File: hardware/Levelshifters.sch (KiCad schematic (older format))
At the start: 36 parts, among them U1401 SN74AXC8T245, U1402 SN74AXC8T245, U1403 SN74AXC8T245, U1404 LSF0102, U1405 LSF0102

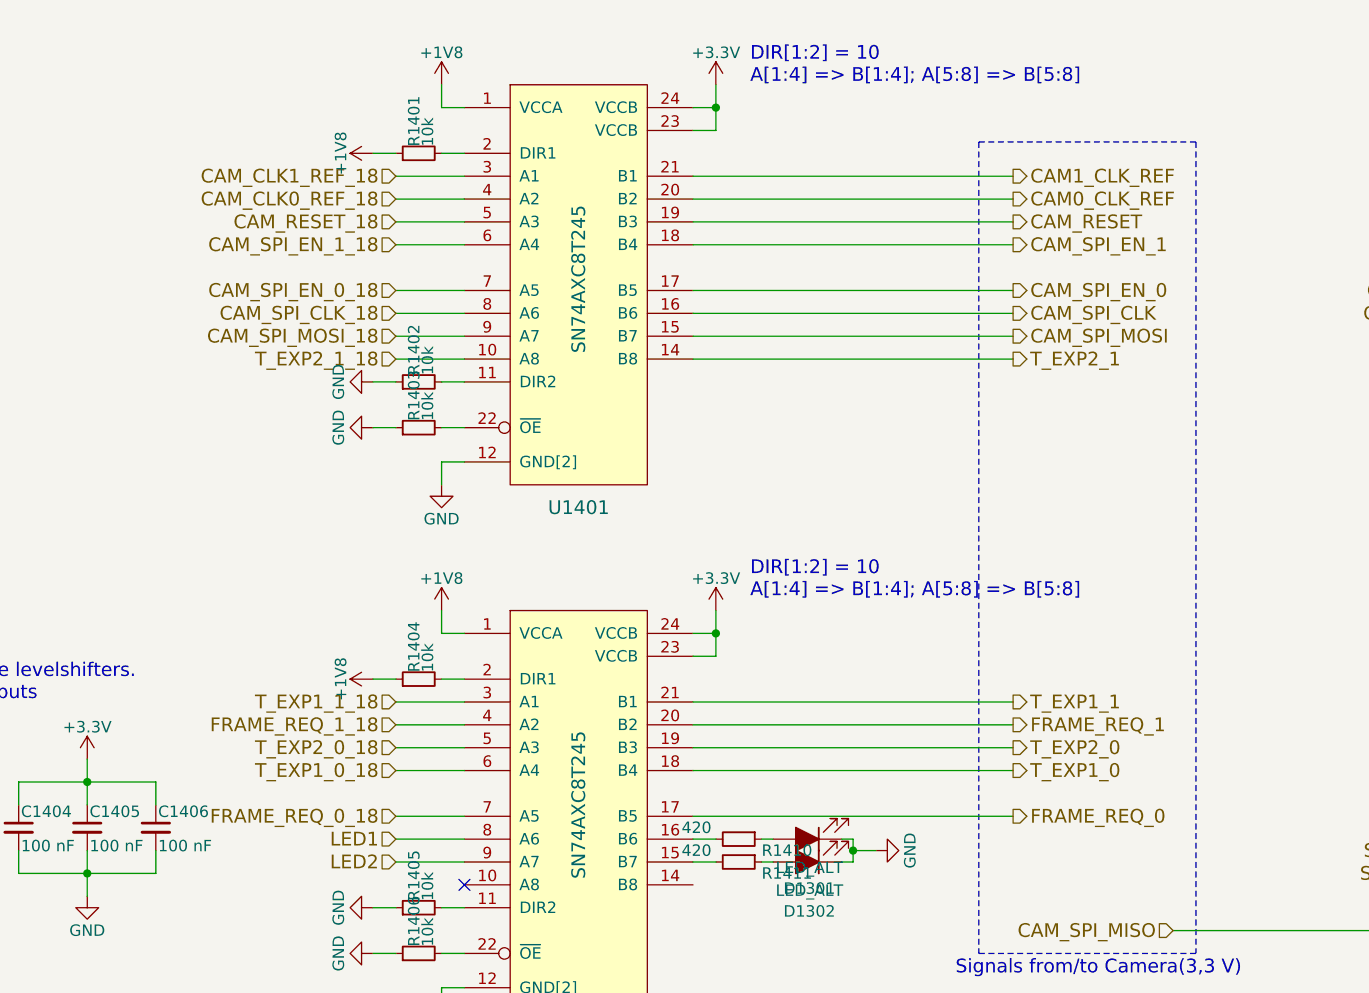
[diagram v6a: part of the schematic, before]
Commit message: WIP: route GPIOs/Levelshifters
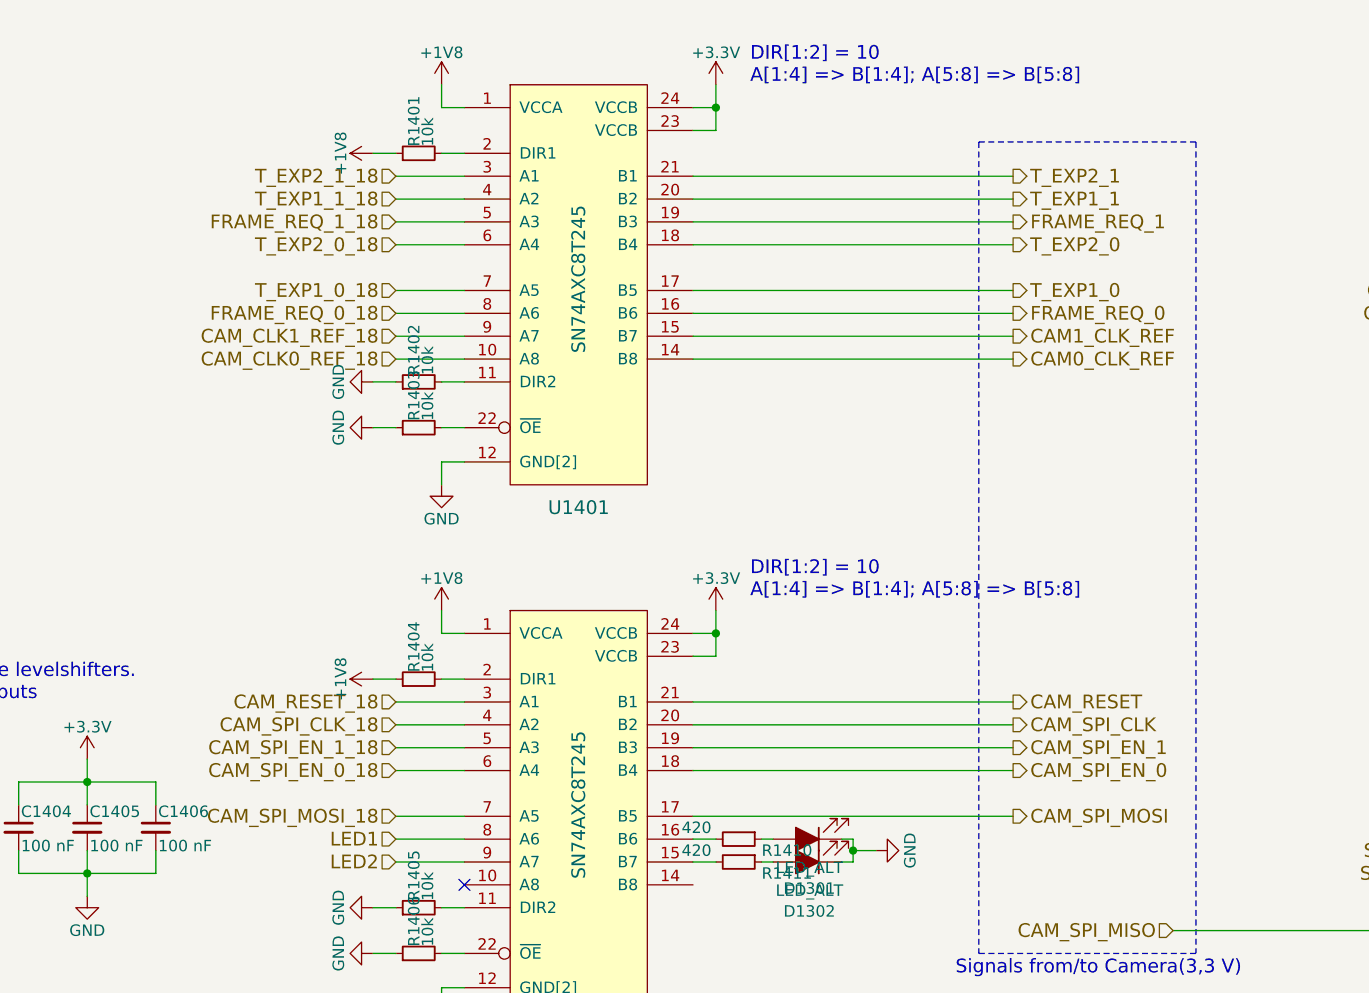
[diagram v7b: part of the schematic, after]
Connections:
- net CAM0_CLK_REF: now also U1401.14 (B8); no longer U1401.20 (B2)
- net CAM1_CLK_REF: now also U1401.15 (B7); no longer U1401.21 (B1)
- net CAM_CLK0_REF_18: now also U1401.10 (A8); no longer U1401.4 (A2)
- net CAM_CLK1_REF_18: now also U1401.9 (A7); no longer U1401.3 (A1)
- net CAM_RESET: now also U1402.21 (B1); no longer U1401.19 (B3)
- net CAM_RESET_18: now also U1402.3 (A1); no longer U1401.5 (A3)
- net CAM_SPI_CLK: now also U1402.20 (B2); no longer U1401.16 (B6)
- net CAM_SPI_CLK_18: now also U1402.4 (A2); no longer U1401.8 (A6)
- net CAM_SPI_EN_0: now also U1402.18 (B4); no longer U1401.17 (B5)
- net CAM_SPI_EN_0_18: now also U1402.6 (A4); no longer U1401.7 (A5)
- net CAM_SPI_EN_1: now also U1402.19 (B3); no longer U1401.18 (B4)
- net CAM_SPI_EN_1_18: now also U1402.5 (A3); no longer U1401.6 (A4)
- net CAM_SPI_MOSI: now also U1402.17 (B5); no longer U1401.15 (B7)
- net CAM_SPI_MOSI_18: now also U1402.7 (A5); no longer U1401.9 (A7)
- net FRAME_REQ_0: now also U1401.16 (B6); no longer U1402.17 (B5)
- net FRAME_REQ_0_18: now also U1401.8 (A6); no longer U1402.7 (A5)
- net FRAME_REQ_1: now also U1401.19 (B3); no longer U1402.20 (B2)
- net FRAME_REQ_1_18: now also U1401.5 (A3); no longer U1402.4 (A2)
- net T_EXP1_0: now also U1401.17 (B5); no longer U1402.18 (B4)
- net T_EXP1_0_18: now also U1401.7 (A5); no longer U1402.6 (A4)
- net T_EXP1_1: now also U1401.20 (B2); no longer U1402.21 (B1)
- net T_EXP1_1_18: now also U1401.4 (A2); no longer U1402.3 (A1)
- net T_EXP2_0: now also U1401.18 (B4); no longer U1402.19 (B3)
- net T_EXP2_0_18: now also U1401.6 (A4); no longer U1402.5 (A3)
- net T_EXP2_1: now also U1401.21 (B1); no longer U1401.14 (B8)
- net T_EXP2_1_18: now also U1401.3 (A1); no longer U1401.10 (A8)
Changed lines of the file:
@@
 Text HLabel 10600 1800 2    60   BiDi ~ 0
 CAM_SCL
+Text HLabel 5950 1900 2    60   Output ~ 0
+FRAME_REQ_0
+Text HLabel 5950 1800 2    60   Output ~ 0
+T_EXP1_0
+Text HLabel 5950 1600 2    60   Output ~ 0
+T_EXP2_0
+Text HLabel 5950 1500 2    60   Output ~ 0
+FRAME_REQ_1
+Text HLabel 5950 1400 2    60   Output ~ 0
+T_EXP1_1
+Text HLabel 5950 1300 2    60   Output ~ 0
+T_EXP2_1
+Text HLabel 5950 3700 2    60   Output ~ 0
+CAM_SPI_CLK
 Text HLabel 5950 4100 2    60   Output ~ 0
-FRAME_REQ_0
-Text HLabel 5950 3900 2    60   Output ~ 0
-T_EXP1_0
-Text HLabel 5950 3800 2    60   Output ~ 0
-T_EXP2_0
-Text HLabel 5950 3700 2    60   Output ~ 0
-FRAME_REQ_1
-Text HLabel 5950 3600 2    60   Output ~ 0
-T_EXP1_1
-Text HLabel 5950 2100 2    60   Output ~ 0
-T_EXP2_1
-Text HLabel 5950 1900 2    60   Output ~ 0
-CAM_SPI_CLK
-Text HLabel 5950 2000 2    60   Output ~ 0
 CAM_SPI_MOSI
 Text HLabel 6650 4600 0    60   Input ~ 0
 CAM_SPI_MISO
-Text HLabel 5950 1800 2    60   Output ~ 0
+Text HLabel 5950 3900 2    60   Output ~ 0
 CAM_SPI_EN_0
-Text HLabel 5950 1600 2    60   Output ~ 0
+Text HLabel 5950 3800 2    60   Output ~ 0
 CAM_SPI_EN_1
-Text HLabel 5950 1300 2    60   Output ~ 0
+Text HLabel 5950 2000 2    60   Output ~ 0
 CAM1_CLK_REF
-Text HLabel 5950 1500 2    60   Output ~ 0
+Text HLabel 5950 3600 2    60   Output ~ 0
 CAM_RESET
 Text Notes 6950 4800 2    60   ~ 0
@@
 Text Notes 4850 5500 0    60   ~ 0
 DIR[1:2] = 01\nA[1:4] <= B[1:4]; A[5:8] => B[5:8]
+Text HLabel 3250 3600 0    60   Input ~ 0
+CAM_RESET_18
+Text HLabel 3250 2000 0    60   Input ~ 0
+CAM_CLK1_REF_18
+Text HLabel 3250 3800 0    60   Input ~ 0
+CAM_SPI_EN_1_18
+Text HLabel 3250 3900 0    60   Input ~ 0
+CAM_SPI_EN_0_18
+Text HLabel 3250 4100 0    60   Input ~ 0
+CAM_SPI_MOSI_18
+Text HLabel 3250 3700 0    60   Input ~ 0
+CAM_SPI_CLK_18
+Text HLabel 3250 1300 0    60   Input ~ 0
+T_EXP2_1_18
+Text HLabel 3250 1400 0    60   Input ~ 0
+T_EXP1_1_18
 Text HLabel 3250 1500 0    60   Input ~ 0
-CAM_RESET_18
-Text HLabel 3250 1300 0    60   Input ~ 0
-CAM_CLK1_REF_18
+FRAME_REQ_1_18
 Text HLabel 3250 1600 0    60   Input ~ 0
-CAM_SPI_EN_1_18
+T_EXP2_0_18
 Text HLabel 3250 1800 0    60   Input ~ 0
-CAM_SPI_EN_0_18
-Text HLabel 3250 2000 0    60   Input ~ 0
-CAM_SPI_MOSI_18
+T_EXP1_0_18
 Text HLabel 3250 1900 0    60   Input ~ 0
-CAM_SPI_CLK_18
-Text HLabel 3250 2100 0    60   Input ~ 0
-T_EXP2_1_18
-Text HLabel 3250 3600 0    60   Input ~ 0
-T_EXP1_1_18
-Text HLabel 3250 3700 0    60   Input ~ 0
-FRAME_REQ_1_18
-Text HLabel 3250 3800 0    60   Input ~ 0
-T_EXP2_0_18
-Text HLabel 3250 3900 0    60   Input ~ 0
-T_EXP1_0_18
-Text HLabel 3250 4100 0    60   Input ~ 0
 FRAME_REQ_0_18
 Text HLabel 3250 5900 0    60   Output ~ 0
@@
 Wire Wire Line
 	3550 4100 3250 4100
-Text HLabel 3250 1400 0    60   Input ~ 0
+Text HLabel 3250 2100 0    60   Input ~ 0
 CAM_CLK0_REF_18
 Wire Wire Line
 	3250 1400 3550 1400
-Text HLabel 5950 1400 2    60   Output ~ 0
+Text HLabel 5950 2100 2    60   Output ~ 0
 CAM0_CLK_REF
 Wire Wire Line

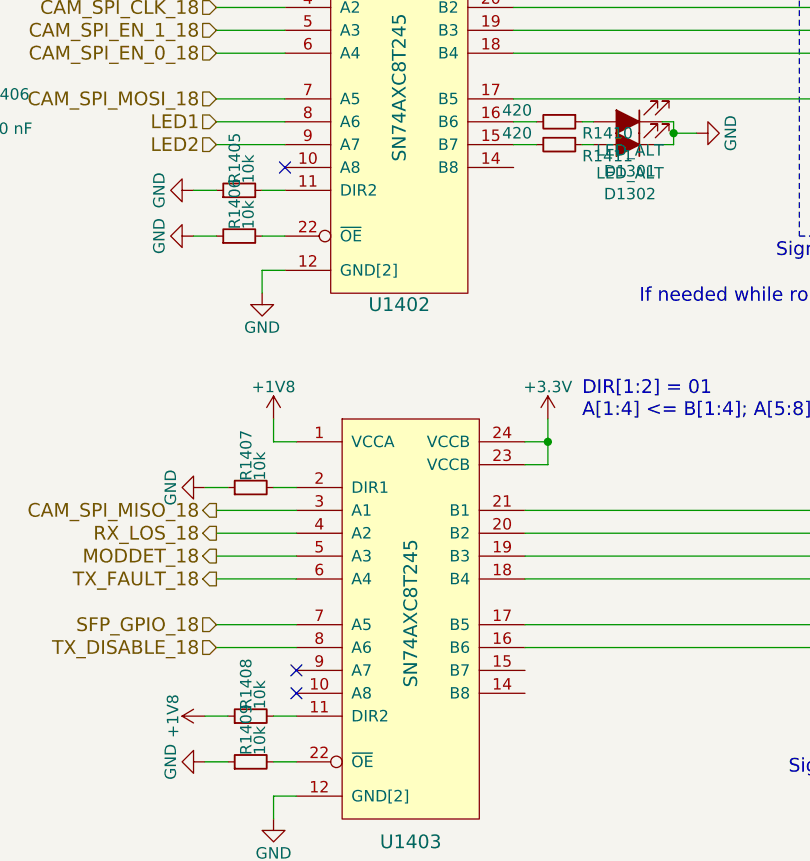
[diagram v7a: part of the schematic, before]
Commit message: WIP: routing the HF Part of the Camera Connector. I have to move the clock away from the left border.
TODO: Fix DDR3 RAM.
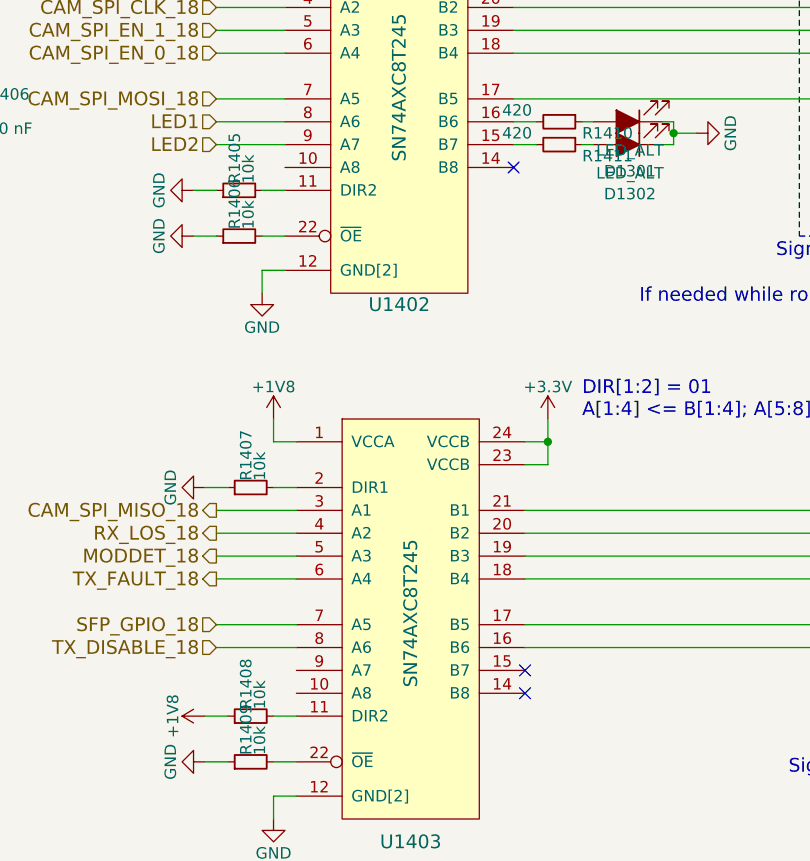
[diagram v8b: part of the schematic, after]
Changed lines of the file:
@@
 	0    1    1    0
 $EndComp
-NoConn ~ 3600 6700
-NoConn ~ 3600 6600
 Text HLabel 3250 6000 0    60   Output ~ 0
 RX_LOS_18
@@
 	1    0    0    -1
 $EndComp
-NoConn ~ 3550 4400
 $Comp
 L lsf0102:LSF0102 U1405
@@
 Wire Wire Line
 	4900 4300 4850 4300
+NoConn ~ 4600 6600
+NoConn ~ 4600 6700
+NoConn ~ 4550 4400
 $EndSCHEMATC
